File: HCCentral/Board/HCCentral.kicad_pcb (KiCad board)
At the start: 2 copper layers, 99.1 x 79.8 mm, 67 parts, among them CON1 BARREL_JACK, CON2 SD_Card, IC1 ENC28J60-I/SO, IC2 ATMEGA1284P-A, J1 RJ45-TRJ0011BANL, P2 ANT_433, P3 ANT_866, P4 ISP, P6 SPI, P7 UART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

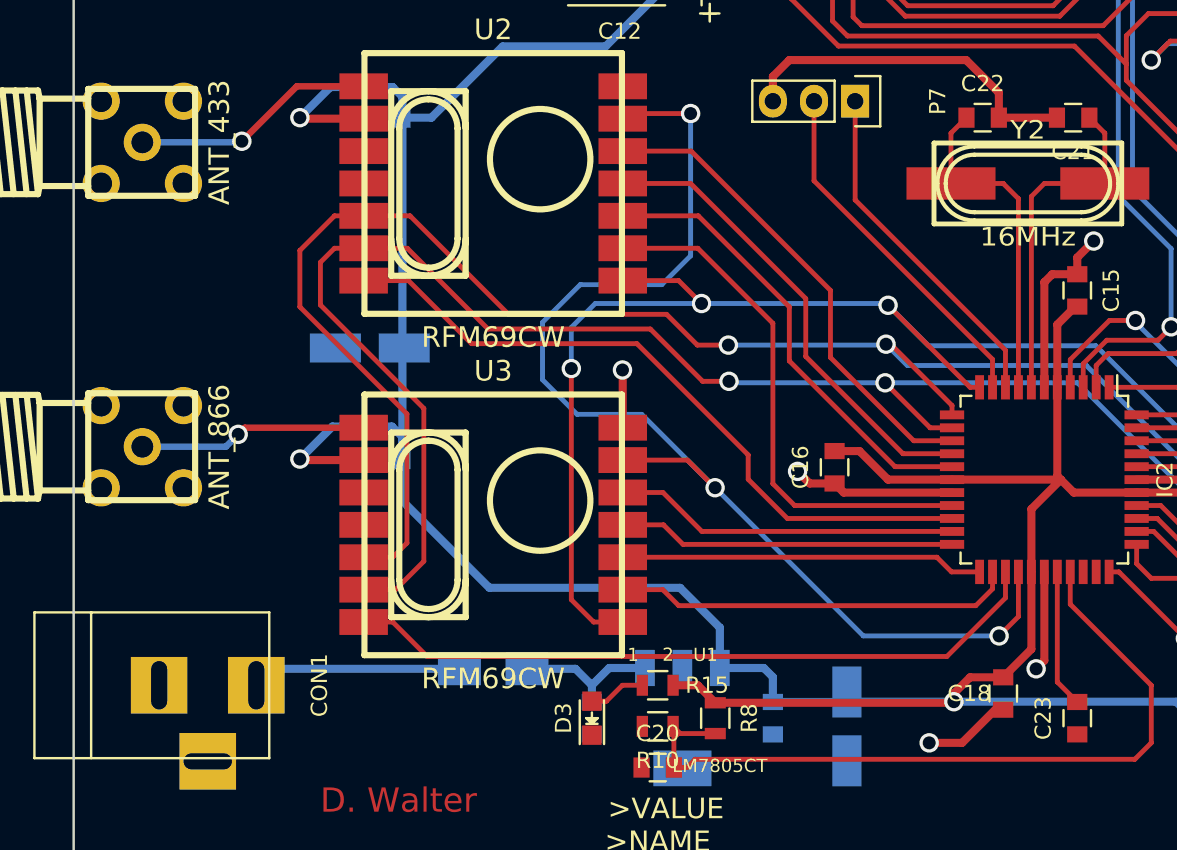
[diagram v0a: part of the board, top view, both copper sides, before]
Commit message: Dateien in richtiges Verzeichnis verschoben
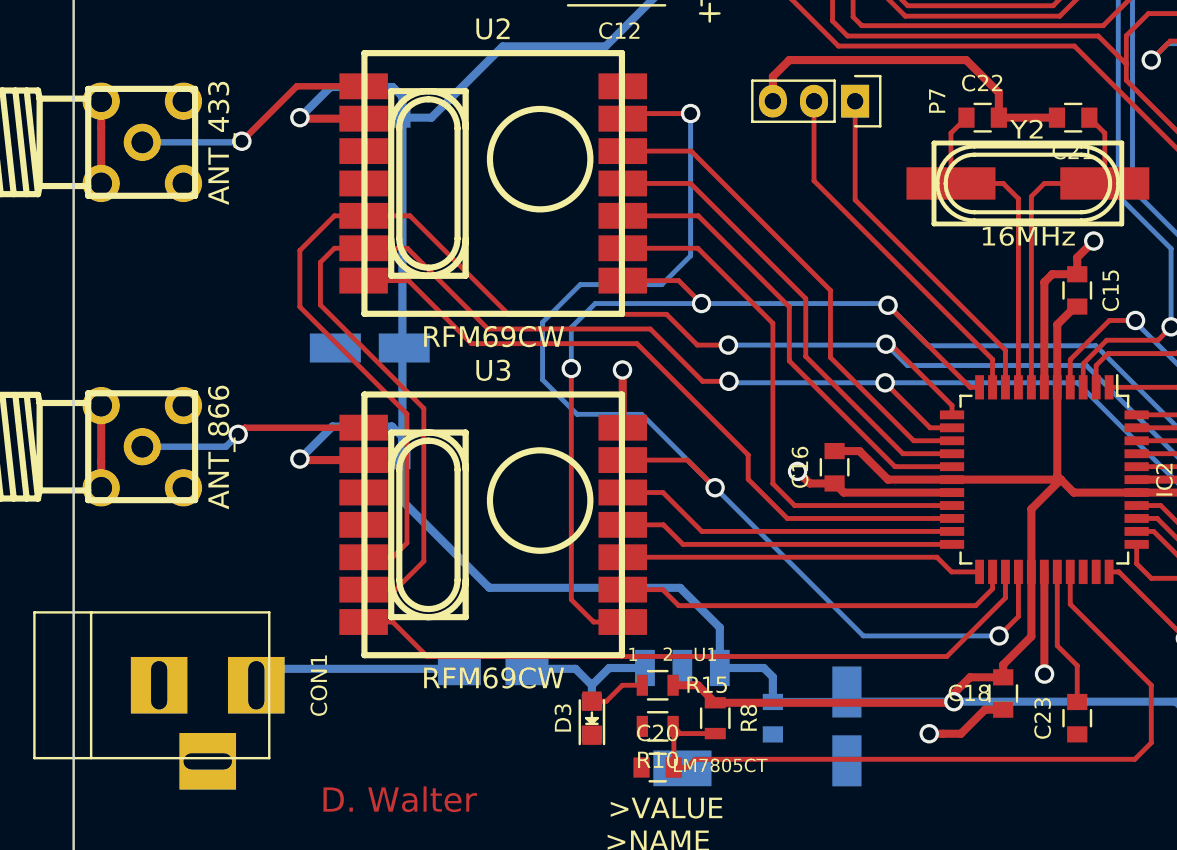
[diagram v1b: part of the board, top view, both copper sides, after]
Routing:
- net GND: track 197.8 -> 207.9 mm
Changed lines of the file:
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@@
   (general
     (links 197)
-    (no_connects 1)
+    (no_connects 0)
     (area 103.048999 50.216999 202.259001 130.123001)
     (thickness 1.6)
     (drawings 11)
-    (tracks 685)
+    (tracks 692)
     (zones 0)
     (modules 67)
@@
   (target plus (at 199.644 52.832) (size 5) (width 0.15) (layer Edge.Cuts))
   (target plus (at 105.664 127.508) (size 5) (width 0.15) (layer Edge.Cuts))
+  (segment (start 104.8258 106.68) (end 104.8258 105.053655) (width 0.5) (layer F.Cu) (net 1))
+  (segment (start 104.8258 105.053655) (end 104.8258 101.6) (width 0.5) (layer F.Cu) (net 1))
+  (segment (start 104.8258 82.804) (end 104.8258 84.430345) (width 0.5) (layer F.Cu) (net 1))
+  (segment (start 104.8258 84.430345) (end 104.8258 87.884) (width 0.5) (layer F.Cu) (net 1))
+  (segment (start 163.068 118.16964) (end 163.080874 118.182514) (width 0.5) (layer F.Cu) (net 1))
+  (segment (start 163.068 111.872) (end 163.068 118.16964) (width 0.5) (layer F.Cu) (net 1))
+  (via (at 163.080874 118.182514) (size 1.2) (drill 0.8) (layers F.Cu B.Cu) (net 1))
+  (segment (start 156.808269 121.865004) (end 155.959741 121.865004) (width 0.5) (layer F.Cu) (net 1))
+  (segment (start 157.917996 121.865004) (end 156.808269 121.865004) (width 0.5) (layer F.Cu) (net 1))
+  (segment (start 159.403 120.38) (end 157.917996 121.865004) (width 0.5) (layer F.Cu) (net 1))
+  (segment (start 160.528 120.38) (end 159.403 120.38) (width 0.5) (layer F.Cu) (net 1))
+  (via (at 155.959741 121.865004) (size 1.2) (drill 0.8) (layers F.Cu B.Cu) (net 1))
   (segment (start 138.033743 66.024) (end 137.584768 65.575025) (width 0.5) (layer F.Cu) (net 1))
   (segment (start 141.224 66.024) (end 138.033743 66.024) (width 0.5) (layer F.Cu) (net 1))
@@
   (segment (start 186.436 120.026389) (end 186.436 118.364) (width 0.5) (layer B.Cu) (net 1))
   (via (at 186.436 118.364) (size 1.2) (drill 0.8) (layers F.Cu B.Cu) (net 1))
-  (segment (start 160.528 120.38) (end 160.036 120.38) (width 0.5) (layer F.Cu) (net 1) (status 30))
-  (segment (start 160.036 120.38) (end 157.988 122.428) (width 0.5) (layer F.Cu) (net 1) (status 10))
-  (segment (start 157.988 122.428) (end 155.956 122.428) (width 0.5) (layer F.Cu) (net 1))
-  (via (at 155.956 122.428) (size 1.2) (drill 0.8) (layers F.Cu B.Cu) (net 1))
   (segment (start 130.572 71.628) (end 129.54 71.628) (width 0.5) (layer F.Cu) (net 1) (status 10))
   (via (at 128.524 70.612) (size 1.2) (drill 0.8) (layers F.Cu B.Cu) (net 1))
   (segment (start 129.54 71.628) (end 128.524 70.612) (width 0.5) (layer F.Cu) (net 1))
-  (segment (start 163.068 111.872) (end 163.068 117.348) (width 0.5) (layer F.Cu) (net 1) (status 10))
-  (segment (start 163.068 117.348) (end 162.56 117.856) (width 0.5) (layer F.Cu) (net 1))
-  (via (at 162.56 117.856) (size 1.2) (drill 0.8) (layers F.Cu B.Cu) (net 1))
   (segment (start 165.1 93.488) (end 165.1 92.456) (width 0.5) (layer F.Cu) (net 1) (status 10))
   (segment (start 165.1 92.456) (end 166.116 91.44) (width 0.5) (layer F.Cu) (net 1))
@@
   (segment (start 174.337 106.172) (end 174.736 106.571) (width 0.5) (layer F.Cu) (net 1))
   (segment (start 174.736 106.571) (end 174.736 107.696) (width 0.5) (layer F.Cu) (net 1) (status 20))
+  (segment (start 162.268 111.872) (end 162.268 115.861226) (width 0.5) (layer F.Cu) (net 2))
+  (segment (start 162.268 115.861226) (end 160.528 117.601226) (width 0.5) (layer F.Cu) (net 2))
+  (segment (start 160.528 117.601226) (end 160.528 118.38) (width 0.5) (layer F.Cu) (net 2))
   (segment (start 123.428 83.82) (end 123.428 97.93402) (width 0.5) (layer B.Cu) (net 2))
   (segment (start 123.428 97.93402) (end 123.53798 98.044) (width 0.5) (layer B.Cu) (net 2))
@@
   (segment (start 123.428 107.482229) (end 123.428 104.902) (width 0.5) (layer B.Cu) (net 2) (status 20))
   (segment (start 123.53798 83.92998) (end 123.428 83.82) (width 0.5) (layer B.Cu) (net 2) (status 30))
-  (segment (start 162.268 116.64) (end 160.528 118.38) (width 0.5) (layer F.Cu) (net 2) (status 20))
-  (segment (start 162.268 111.872) (end 162.268 116.64) (width 0.5) (layer F.Cu) (net 2) (status 10))
   (segment (start 153.416 106.172) (end 151.654 104.41) (width 0.5) (layer F.Cu) (net 2))
   (segment (start 151.654 104.41) (end 150.114 104.41) (width 0.5) (layer F.Cu) (net 2) (status 20))
@@
   (segment (start 157.988 88.5698) (end 157.3022 87.884) (width 0.3) (layer F.Cu) (net 41) (status 30))
   (segment (start 158.496 88.0618) (end 158.3182 87.884) (width 0.3) (layer F.Cu) (net 41) (status 30))
-  (segment (start 163.868 111.872) (end 163.868 118.672) (width 0.3) (layer F.Cu) (net 42) (status 10))
-  (segment (start 163.868 118.672) (end 165.1 119.904) (width 0.3) (layer F.Cu) (net 42) (status 20))
+  (segment (start 163.868 111.872) (end 163.868 116.429307) (width 0.3) (layer F.Cu) (net 42))
+  (segment (start 163.868 116.429307) (end 165.1 117.661307) (width 0.3) (layer F.Cu) (net 42))
+  (segment (start 165.1 117.661307) (end 165.1 119.904) (width 0.3) (layer F.Cu) (net 42))
   (segment (start 168.768 104.572) (end 183.464 104.572) (width 0.3) (layer F.Cu) (net 43) (status 10))
   (segment (start 176.005 62.467) (end 172.212 62.467) (width 0.3) (layer F.Cu) (net 43) (status 20))

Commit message: Layouting...
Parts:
- added G***: LOGO, Loewe:Loewe_Klein, F.Cu at (108.7, 94.7)
- moved J1 0.84 mm to (112.1, 65.5)
- moved P2 0.84 mm to (104.0, 85.3)
- moved P3 0.84 mm to (104.0, 104.1)
- moved D1 0.76 mm to (199.9, 101.1)
- moved D2 0.76 mm to (199.9, 94.5)
- moved D4 0.76 mm to (199.9, 88.4)
- moved SW1 0.25 mm to (199.4, 120.9)
- moved SW2 0.25 mm to (199.4, 110.2)
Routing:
- net GND: track 207.9 -> 197.1 mm
- net Net-(IC1-Pad13): track 51.4 -> 49.3 mm
- net Net-(C19-Pad2): track 53.6 -> 55.0 mm
- net /Controller_USB_SD/MISO_LAN: track 65.5 -> 64.3 mm
- net Net-(IC1-Pad26): track 67.0 -> 67.9 mm
- net /Controller_USB_SD/MOSI_LAN: track 84.5 -> 83.6 mm
- net Net-(IC1-Pad17): track 59.3 -> 58.4 mm
- net Net-(C10-Pad2): track 26.4 -> 25.6 mm
- net /Controller_USB_SD/SCK_LAN: track 62.1 -> 62.9 mm
- net Net-(D4-Pad2): track 3.62 -> 2.86 mm
- net Net-(D2-Pad2): track 3.62 -> 2.86 mm
- net Net-(D1-Pad2): track 3.62 -> 2.86 mm
- net Net-(IC1-Pad16): track 54.4 -> 53.7 mm
- net Net-(IC1-Pad12): track 48.4 -> 47.7 mm
- net +3V3: track 388.8 -> 388.3 mm
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
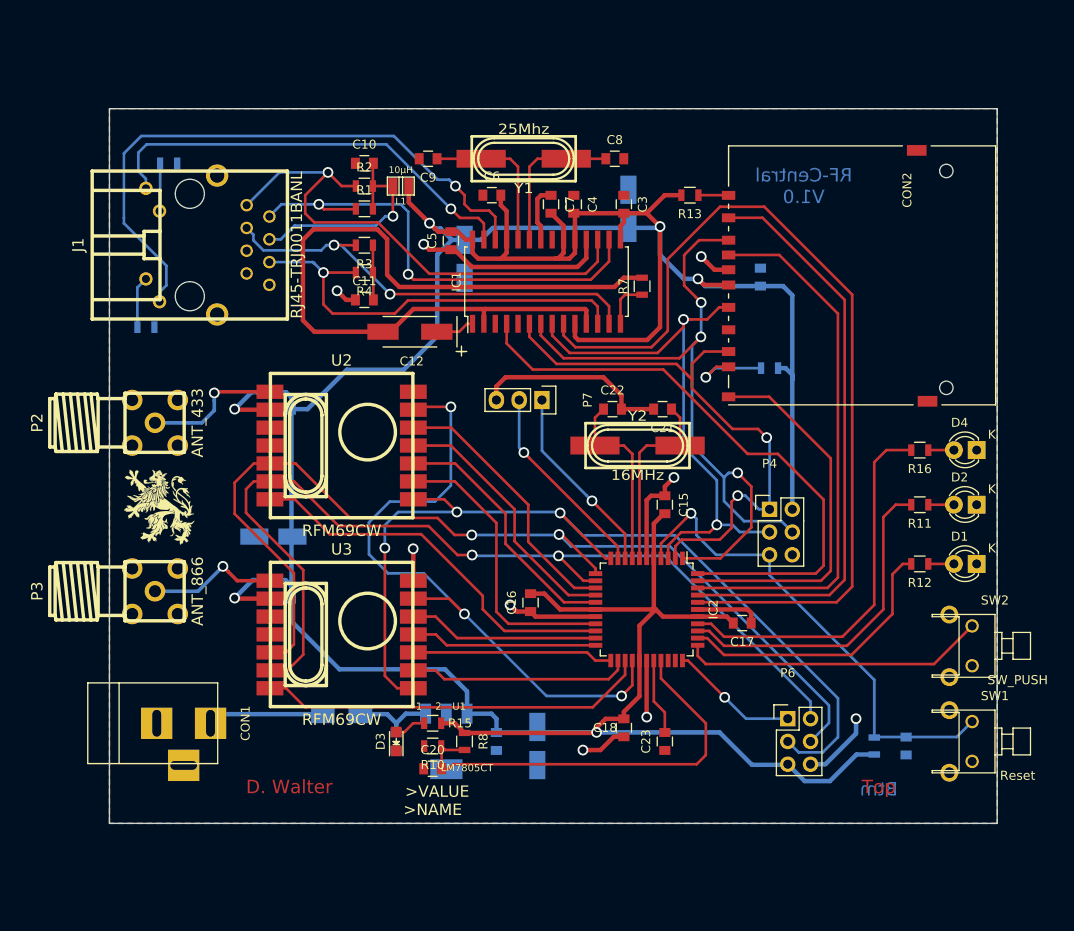
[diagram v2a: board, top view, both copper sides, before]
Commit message: PiShield neu angelegt
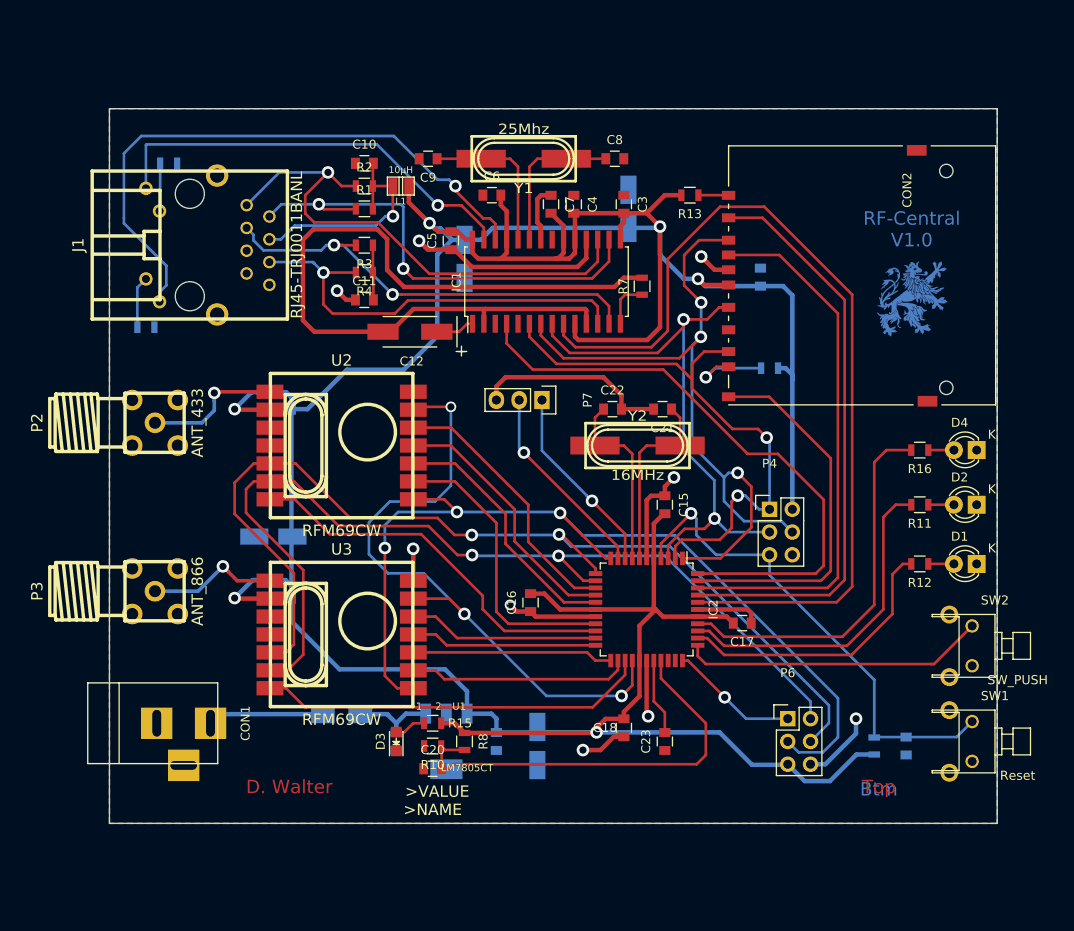
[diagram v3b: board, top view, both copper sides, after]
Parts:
- removed G***: LOGO, Loewe:Loewe_Klein
- added ?: , Loewe:Loewe_klein_CU, B.Cu at (192.7, 71.5)
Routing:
- net Net-(IC1-Pad27): track 48.7 -> 47.7 mm
- net Net-(IC1-Pad26): track 67.9 -> 67.3 mm
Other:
- net class Antenna: via_dia 1.2 -> 1.4
- net class Default: via_dia 1.2 -> 1.4
- net class Power: via_dia 1.2 -> 1.4

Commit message: Layout aktualisiert, 10x10cm
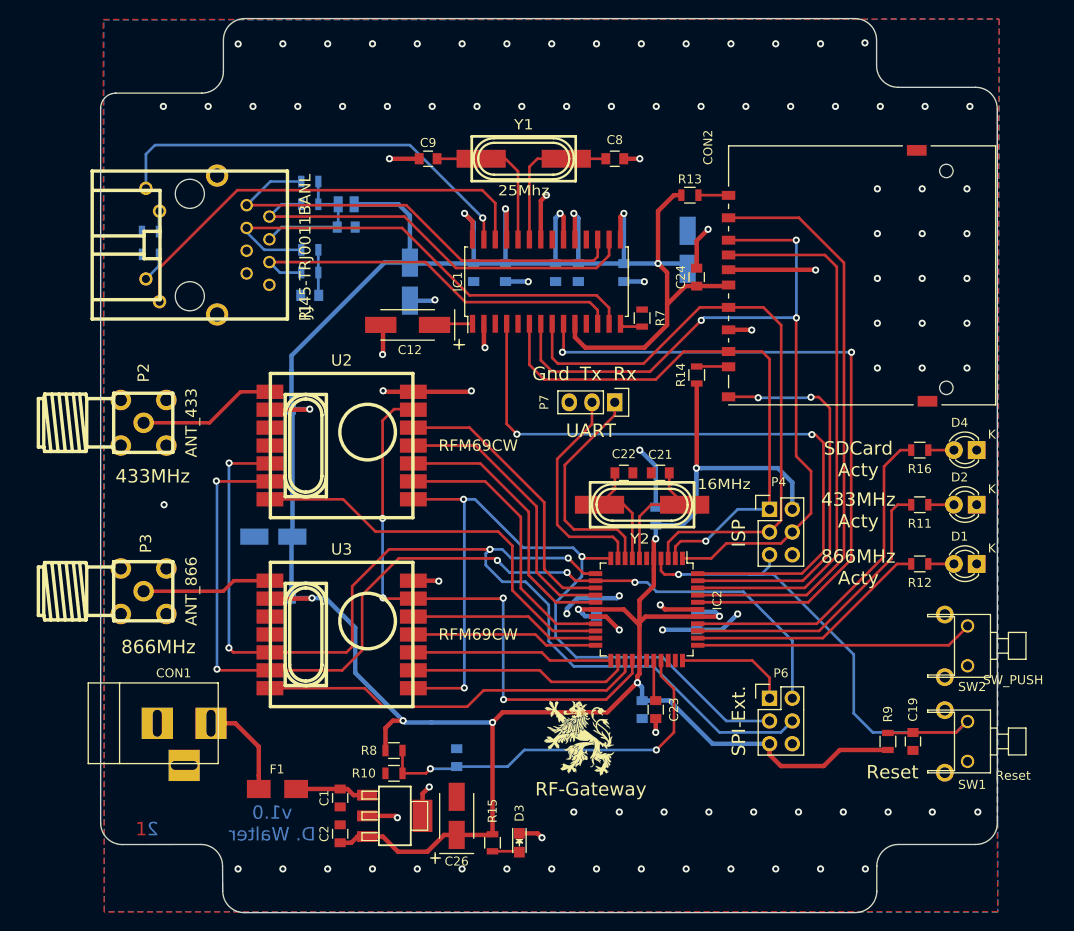
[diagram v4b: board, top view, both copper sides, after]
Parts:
- removed the ? at (192.7, 71.5)
- added ?: , Loewe:Loewe_Klein, F.Cu at (155.6, 120.5)
- C1, C19, C2, C24, C26, F1, R14, R9, U1: moved to F.Cu
- C10, C11, C15, C16, C17, C18, C20, C3, C4, C5, C6, C7, L1, R1, R2, R3, R4: moved to B.Cu
- moved C2 20.3 mm to (128.9, 131.2), turned to 90 degrees
- moved D3 17.8 mm to (148.9, 132.2), turned to 270 degrees
- moved R15 14.9 mm to (145.9, 132.2), turned to 270 degrees
- moved C26 11.9 mm to (141.9, 129.2), turned to 90 degrees
- moved F1 11.0 mm to (121.9, 126.2)
- moved U1 10.1 mm to (135.0, 129.2), turned to 270 degrees
- moved C1 8.88 mm to (128.9, 127.2)
- moved C6 8.77 mm to (147.3, 68.6), turned to 90 degrees
- moved R14 8.16 mm to (168.7, 80.0), turned to 270 degrees
- moved R6 8.14 mm to (107.7, 66.5), turned to 0 degrees
- moved P7 8.13 mm to (159.5, 83.1)
- moved C25 8.03 mm to (167.6, 66.0)
- moved R8 7.94 mm to (134.9, 121.9), turned to 0 degrees
- moved R5 7.89 mm to (107.7, 64.0), turned to 0 degrees
- moved C4 7.64 mm to (155.4, 68.6), turned to 90 degrees
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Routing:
- net GND: track 197.4 -> 95.4 mm, vias 9 -> 25
- net /Controller_USB_SD/CS_LAN: track 99.9 -> 77.7 mm, vias 0 -> 2
- net Net-(IC1-Pad26): track 67.3 -> 49.5 mm, vias 1 -> 0
- net /Controller_USB_SD/MISO_RF: track 104.7 -> 90.0 mm
- net +3V3: track 388.3 -> 376.2 mm, vias 6 -> 15
- net Net-(C10-Pad2): track 25.6 -> 15.5 mm, vias 1 -> 0
- net Net-(C21-Pad1): track 24.3 -> 14.5 mm
- net Net-(C22-Pad1): track 23.0 -> 13.4 mm
- net /Controller_USB_SD/MOSI_RF: track 113.5 -> 123.0 mm, vias 2 -> 4
- net /Controller_USB_SD/IRQ_LAN: track 66.6 -> 74.6 mm, vias 0 -> 2
- net /Controller_USB_SD/SCK_LAN: track 62.7 -> 70.2 mm, vias 2 -> 0
- net /Controller_USB_SD/Reset_RF: track 73.1 -> 65.6 mm, vias 3 -> 4
- net Net-(IC1-Pad17): track 58.4 -> 51.0 mm, vias 1 -> 0
- net /Controller_USB_SD/MOSI_LAN: track 83.6 -> 90.8 mm
- net Net-(IC1-Pad16): track 53.6 -> 46.8 mm, vias 2 -> 0
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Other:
- board size 99.1 x 79.8 mm -> 100.1 x 99.8 mm
- net class Antenna: via_dia 1.4 -> 0.8; via_drill 0.8 -> 0.4
- net class Default: via_dia 1.4 -> 0.8; via_drill 0.8 -> 0.4
- net class Power: via_dia 1.4 -> 0.8; via_drill 0.8 -> 0.4
- board text added: "1"
- board text added: "2"
- board text added: "433MHz"
- board text added: "433MHz Acty"
- board text added: "866MHz"
- board text added: "866MHz Acty"
- board text added: "Gnd"
- board text added: "ISP"
- board text added: "RF-Gateway"
- board text added: "Reset"
- board text added: "Rx"
- board text added: "SDCard Acty"
- board text added: "SPI-Ext."
- board text added: "Tx"
- board text added: "UART"
- board text added: "v1.0 D. Walter"
- board text removed: "Btm"
- board text removed: "D. Walter"
- board text removed: "RF-Central V1.0"
- board text removed: "Top"

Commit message: Layout zur Fertigung
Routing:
- net GND: track 95.4 -> 502.6 mm, vias 25 -> 100
- net (no net): vias 75 -> 1
